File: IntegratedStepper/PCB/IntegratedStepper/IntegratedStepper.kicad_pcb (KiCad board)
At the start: 4 copper layers, 57 x 42.5 mm, 76 parts, among them IC1 DRV8844PWPR, IC2 SN65HVD230DR, IC3 LMR38020FSQDDARQ1, J1 8P8C, J2 8P8C, J3 Screw_Terminal_01x02, J4 Screw_Terminal_01x02, J5 Conn_01x05_Socket, Q1 SS8050-G, Q2 SS8050-G, U1 ESP32-WROOM-32E, U2 AS5048A, U3 CP2102N-Axx-xQFN28

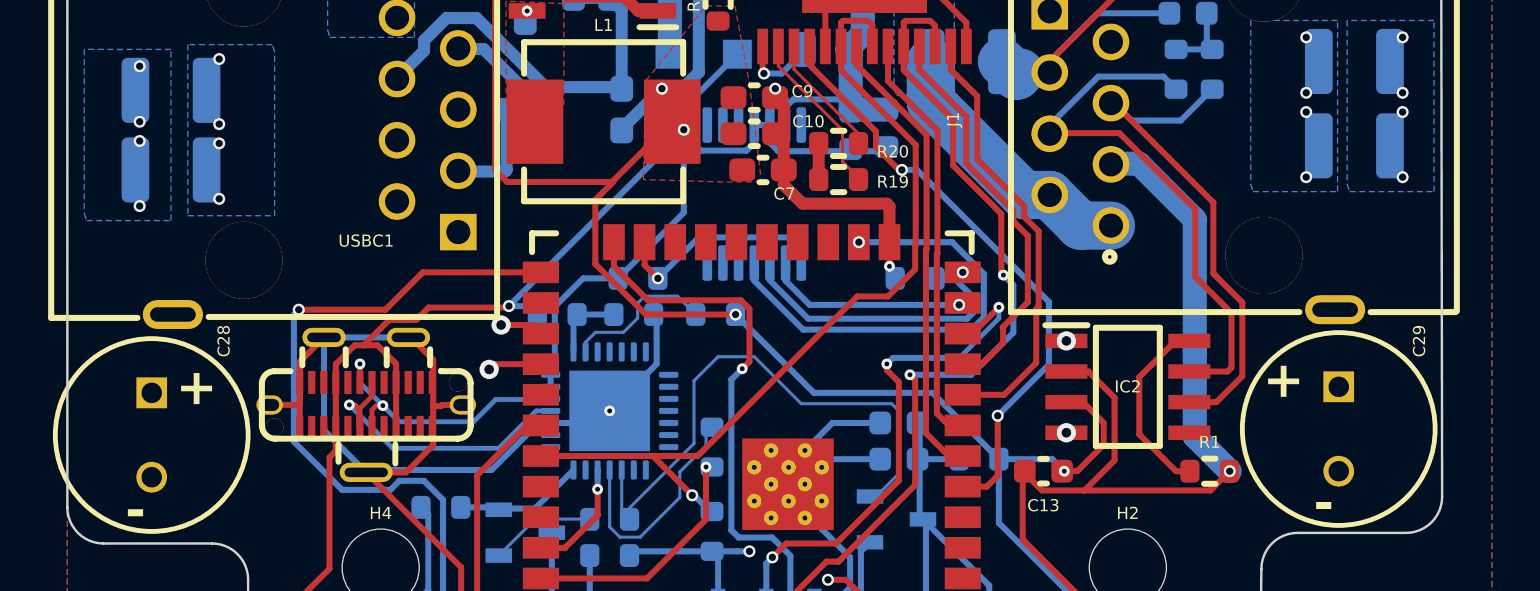
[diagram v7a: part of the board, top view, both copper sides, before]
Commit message: Update schem + PCB with learnings from bringup
PU resistors for DRV8844 were on a 3V3 island and were NOT pulled up :L
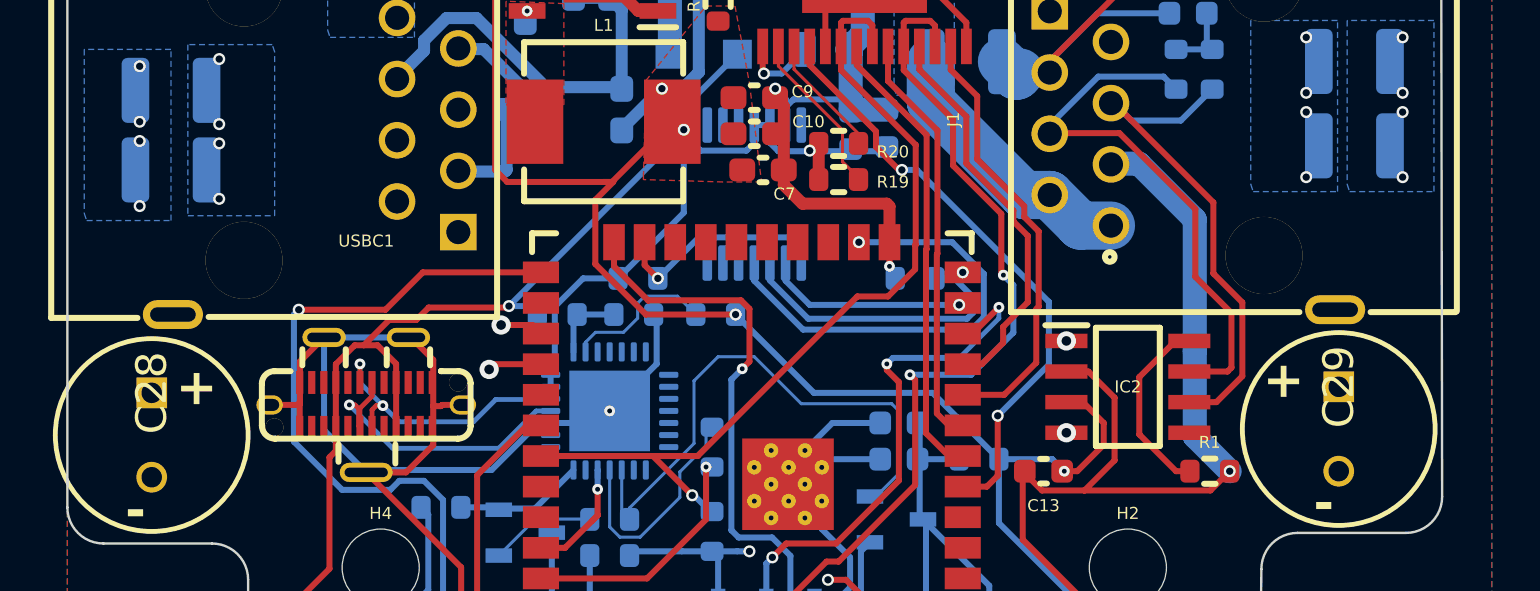
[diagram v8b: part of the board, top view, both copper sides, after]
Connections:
- net /DRV8844/EN4 renamed /DRV8844/EN3
- R19 pad 1: /DRV8844/3V3_VCC -> 3V3_VCC
- R20 pad 1: /DRV8844/3V3_VCC -> 3V3_VCC
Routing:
- net 3V3_VCC: track 140.1 -> 141.2 mm, vias 7 -> 8
- net /DRV8844/3V3_VCC: track 1.10 -> 0.00 mm
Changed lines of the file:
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@@
 	(net 52 "/ESP32_MCU/M_CS0")
 	(net 53 "/ESP32_MCU/M_MISO")
-	(net 54 "/DRV8844/3V3_VCC")
+	(net 54 "/DRV8844/EN3")
 	(net 55 "Net-(VM1-K)")
 	(net 56 "Net-(V3v3-K)")
@@
 	(net 116 "unconnected-(IC3-PG-Pad6)")
 	(net 117 "/DRV8844/EN1")
-	(net 118 "/DRV8844/EN4")
 	(footprint "Capacitor_SMD:C_0603_1608Metric_Pad1.08x0.95mm_HandSolder"
 		(layer "F.Cu")
@@
 			(size 0.45 1.475)
 			(layers "F.Cu" "F.Paste" "F.Mask")
-			(net 118 "/DRV8844/EN4")
+			(net 54 "/DRV8844/EN3")
 			(pinfunction "EN4")
 			(pintype "passive")
@@
 			(size 0.45 1.475)
 			(layers "F.Cu" "F.Paste" "F.Mask")
-			(net 118 "/DRV8844/EN4")
+			(net 54 "/DRV8844/EN3")
 			(pinfunction "EN3")
 			(pintype "passive")
@@
 			(layers "F.Cu" "F.Paste" "F.Mask")
 			(roundrect_rratio 0.25)
-			(net 54 "/DRV8844/3V3_VCC")
+			(net 8 "3V3_VCC")
 			(pintype "passive")
 		)
@@
 		(tags "Capacitor Polarised")
 		(property "Reference" "C29"
-			(at -1.9 -3.35 -90)
+			(at 0 0 -90)
 			(layer "F.SilkS")
 			(effects
 				(font
-					(size 0.5 0.5)
-					(thickness 0.125)
+					(size 1.27 1.27)
+					(thickness 0.254)
 				)
 			)
@@
 		(tags "Capacitor Polarised")
 		(property "Reference" "C28"
-			(at -2.15 -3 -90)
+			(at 0 0 -90)
 			(layer "F.SilkS")
 			(effects
 				(font
-					(size 0.5 0.5)
-					(thickness 0.125)
+					(size 1.27 1.27)
+					(thickness 0.254)
 				)
 			)
@@
 			(layers "F.Cu" "F.Paste" "F.Mask")
 			(roundrect_rratio 0.25)
-			(net 54 "/DRV8844/3V3_VCC")
+			(net 8 "3V3_VCC")
 			(pintype "passive")
 		)
@@
 			(size 1.5 0.9)
 			(layers "F.Cu" "F.Paste" "F.Mask")
-			(net 118 "/DRV8844/EN4")
+			(net 54 "/DRV8844/EN3")
 			(pinfunction "IO19")
 			(pintype "bidirectional")
@@
 			(layers "B.Cu" "B.Paste" "B.Mask")
 			(roundrect_rratio 0.25)
-			(net 118 "/DRV8844/EN4")
+			(net 54 "/DRV8844/EN3")
 			(pintype "passive")
 		)
@@
 	)
 	(segment
+		(start 123.675 118.9)
+		(end 123.675 120)
+		(width 0.5)
+		(layer "F.Cu")
+		(net 8)
+	)
+	(segment
 		(start 134.3625 141)
 		(end 132.8525 139.49)
@@
 		(net 8)
 	)
+	(via
+		(at 123.3 119.2)
+		(size 0.5)
+		(drill 0.3)
+		(layers "F.Cu" "B.Cu")
+		(net 8)
+	)
 	(segment
 		(start 121.867537 137.00571)
@@
 	)
 	(segment
-		(start 123.675 118.9)
-		(end 123.675 120)
-		(width 0.5)
+		(start 127.7 118.9635)
+		(end 127.7 123.102208)
+		(width 0.25)
+		(layer "F.Cu")
+		(net 54)
+	)
+	(segment
+		(start 124.6 114.876)
+		(end 124.6 113.8885)
+		(width 0.25)
+		(layer "F.Cu")
+		(net 54)
+	)
+	(segment
+		(start 124.6755 113.813)
+		(end 125.713 113.813)
+		(width 0.25)
+		(layer "F.Cu")
+		(net 54)
+	)
+	(segment
+		(start 125.713 113.813)
+		(end 125.9 114)
+		(width 0.25)
+		(layer "F.Cu")
+		(net 54)
+	)
+	(segment
+		(start 124.6 114.876)
+		(end 124.6 115.8635)
+		(width 0.25)
 		(layer "F.Cu")
 		(net 54)
 	)
 	(segment
+		(start 125.275 125.25)
+		(end 118.655 131.87)
+		(width 0.25)
+		(layer "F.Cu")
+		(net 54)
+	)
+	(segment
+		(start 124.6 113.8885)
+		(end 124.6755 113.813)
+		(width 0.25)
+		(layer "F.Cu")
+		(net 54)
+	)
+	(segment
+		(start 118.655 131.87)
+		(end 116.795 131.87)
+		(width 0.25)
+		(layer "F.Cu")
+		(net 54)
+	)
+	(segment
+		(start 126.55 125.25)
+		(end 125.275 125.25)
+		(width 0.25)
+		(layer "F.Cu")
+		(net 54)
+	)
+	(segment
+		(start 124.6 115.8635)
+		(end 127.7 118.9635)
+		(width 0.25)
+		(layer "F.Cu")
+		(net 54)
+	)
+	(segment
+		(start 116.795 131.87)
+		(end 112.15 131.87)
+		(width 0.25)
+		(layer "F.Cu")
+		(net 54)
+	)
+	(segment
+		(start 125.9 114)
+		(end 125.9 114.876)
+		(width 0.25)
+		(layer "F.Cu")
+		(net 54)
+	)
+	(segment
+		(start 127.7 123.102208)
+		(end 127.675 123.127208)
+		(width 0.25)
+		(layer "F.Cu")
+		(net 54)
+	)
+	(segment
+		(start 127.675 124.125)
+		(end 126.55 125.25)
+		(width 0.25)
+		(layer "F.Cu")
+		(net 54)
+	)
+	(segment
+		(start 127.675 123.127208)
+		(end 127.675 124.125)
+		(width 0.25)
+		(layer "F.Cu")
+		(net 54)
+	)
+	(segment
+		(start 118.425 133.5)
+		(end 116.795 131.87)
+		(width 0.25)
+		(layer "F.Cu")
+		(net 54)
+	)
+	(via
+		(at 118.425 133.5)
+		(size 0.5)
+		(drill 0.3)
+		(layers "F.Cu" "B.Cu")
+		(net 54)
+	)
+	(segment
+		(start 118.5 133.5)
+		(end 119.175 134.175)
+		(width 0.25)
+		(layer "B.Cu")
+		(net 54)
+	)
+	(segment
+		(start 118.425 133.5)
+		(end 118.5 133.5)
+		(width 0.25)
+		(layer "B.Cu")
+		(net 54)
+	)
+	(segment
 		(start 137.35 101)
 		(end 135.7875 101)
@@
 		(net 117)
 	)
-	(segment
-		(start 127.7 118.9635)
-		(end 127.7 123.102208)
-		(width 0.25)
-		(layer "F.Cu")
-		(net 118)
-	)
-	(segment
-		(start 124.6 114.876)
-		(end 124.6 113.8885)
-		(width 0.25)
-		(layer "F.Cu")
-		(net 118)
-	)
-	(segment
-		(start 124.6755 113.813)
-		(end 125.713 113.813)
-		(width 0.25)
-		(layer "F.Cu")
-		(net 118)
-	)
-	(segment
-		(start 125.713 113.813)
-		(end 125.9 114)
-		(width 0.25)
-		(layer "F.Cu")
-		(net 118)
-	)
-	(segment
-		(start 124.6 114.876)
-		(end 124.6 115.8635)
-		(width 0.25)
-		(layer "F.Cu")
-		(net 118)
-	)
-	(segment
-		(start 125.275 125.25)
-		(end 118.655 131.87)
-		(width 0.25)
-		(layer "F.Cu")
-		(net 118)
-	)
-	(segment
-		(start 124.6 113.8885)
-		(end 124.6755 113.813)
-		(width 0.25)
-		(layer "F.Cu")
-		(net 118)
-	)
-	(segment
-		(start 118.655 131.87)
-		(end 116.795 131.87)
-		(width 0.25)
-		(layer "F.Cu")
-		(net 118)
-	)
-	(segment
-		(start 126.55 125.25)
-		(end 125.275 125.25)
-		(width 0.25)
-		(layer "F.Cu")
-		(net 118)
-	)
-	(segment
-		(start 124.6 115.8635)
-		(end 127.7 118.9635)
-		(width 0.25)
-		(layer "F.Cu")
-		(net 118)
-	)
-	(segment
-		(start 116.795 131.87)
-		(end 112.15 131.87)
-		(width 0.25)
-		(layer "F.Cu")
-		(net 118)
-	)
-	(segment
-		(start 125.9 114)
-		(end 125.9 114.876)
-		(width 0.25)
-		(layer "F.Cu")
-		(net 118)
-	)
-	(segment
-		(start 127.7 123.102208)
-		(end 127.675 123.127208)
-		(width 0.25)
-		(layer "F.Cu")
-		(net 118)
-	)
-	(segment
-		(start 127.675 124.125)
-		(end 126.55 125.25)
-		(width 0.25)
-		(layer "F.Cu")
-		(net 118)
-	)
-	(segment
-		(start 127.675 123.127208)
-		(end 127.675 124.125)
-		(width 0.25)
-		(layer "F.Cu")
-		(net 118)
-	)
-	(segment
-		(start 118.425 133.5)
-		(end 116.795 131.87)
-		(width 0.25)
-		(layer "F.Cu")
-		(net 118)
-	)
-	(via
-		(at 118.425 133.5)
-		(size 0.5)
-		(drill 0.3)
-		(layers "F.Cu" "B.Cu")
-		(net 118)
-	)
-	(segment
-		(start 118.5 133.5)
-		(end 119.175 134.175)
-		(width 0.25)
-		(layer "B.Cu")
-		(net 118)
-	)
-	(segment
-		(start 118.425 133.5)
-		(end 118.5 133.5)
-		(width 0.25)
-		(layer "B.Cu")
-		(net 118)
-	)
 	(zone
